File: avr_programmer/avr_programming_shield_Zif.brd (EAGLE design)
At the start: 68.6 x 53.3 mm, 16 parts

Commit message: Update after lunch session.
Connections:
- removed net N$22: ISP_85.6, U$2.3
- net N$18: now also ISP_85.6
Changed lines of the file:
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@@
 <wire x1="38.0873" y1="14.0843" x2="33.02" y2="13.9954" width="0" layer="19" extent="1-1"/>
 <wire x1="43.18" y1="13.9954" x2="38.0873" y2="14.0843" width="0" layer="19" extent="1-1"/>
+<wire x1="48.26" y1="13.97" x2="43.18" y2="13.9954" width="0" layer="19" extent="1-1"/>
+<wire x1="55.7276" y1="6.7818" x2="48.26" y2="13.97" width="0" layer="19" extent="1-1"/>
+<wire x1="62.23" y1="6.7818" x2="55.7276" y2="6.7818" width="0" layer="19" extent="1-1"/>
 <wire x1="43.561" y1="2.54" x2="43.18" y2="13.9954" width="0" layer="19" extent="1-1"/>
 <wire x1="41.021" y1="2.54" x2="43.561" y2="2.54" width="0" layer="19" extent="1-1"/>
-<wire x1="55.7276" y1="6.7818" x2="43.561" y2="2.54" width="0" layer="19" extent="1-1"/>
-<wire x1="62.23" y1="6.7818" x2="55.7276" y2="6.7818" width="0" layer="19" extent="1-1"/>
-<wire x1="48.26" y1="13.97" x2="33.02" y2="13.9954" width="0" layer="19" extent="1-1"/>
 </signal>
 <signal name="RESET">
@@
 <contactref element="ISP_84" pad="5"/>
 <contactref element="U$2" pad="4"/>
-<wire x1="34.29" y1="35.56" x2="52.07" y2="21.59" width="0" layer="19" extent="1-1"/>
+<contactref element="ISP_85" pad="6"/>
+<wire x1="45.72" y1="21.59" x2="52.07" y2="21.59" width="0" layer="19" extent="1-1"/>
+<wire x1="34.29" y1="35.56" x2="45.72" y2="21.59" width="0" layer="19" extent="1-1"/>
 </signal>
 <signal name="N$19">
@@
 <wire x1="29.21" y1="43.18" x2="43.18" y2="24.13" width="0" layer="19" extent="1-1"/>
 </signal>
-<signal name="N$22">
-<contactref element="ISP_85" pad="6"/>
-<contactref element="U$2" pad="3"/>
-<wire x1="31.75" y1="35.56" x2="45.72" y2="21.59" width="0" layer="19" extent="1-1"/>
-</signal>
 <signal name="N$14">

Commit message: Added reset cap and resonator, fixed ISP_84 MISO line.
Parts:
- added 16MHZ: RESONATORPTH, SparkFun:RESONATOR-PTH
- added C1: 10uF, SparkFun:CPOL-RADIAL-10UF-25V
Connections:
- new net N$22: 16MHZ.1, U$2.9
- new net N$25: 16MHZ.3, U$2.10
- net GND: now also 16MHZ.2
- net RESET: now also C1.2
- net VCC: now also C1.1
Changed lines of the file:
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@@
 <setting verticaltext="up"/>
 </settings>
-<grid distance="0.05" unitdist="inch" unit="inch" style="lines" multiple="1" display="yes" altdistance="0.0005" altunitdist="inch" altunit="inch"/>
+<grid distance="0.05" unitdist="inch" unit="inch" style="lines" multiple="1" display="yes" altdistance="0.005" altunitdist="inch" altunit="inch"/>
 <layers>
 <layer number="1" name="Top" color="4" fill="1" visible="yes" active="yes"/>
@@
 <element name="BNK" library="adafruit" package="LED3MM" value="" x="48.26" y="10.16" rot="R90"/>
 <element name="R4" library="adafruit" package="0204V" value="" x="49.53" y="13.97"/>
+<element name="C1" library="SparkFun" package="CPOL-RADIAL-10UF-25V" value="10uF" x="-8.89" y="3.81"/>
+<element name="16MHZ" library="SparkFun" package="RESONATOR-PTH" value="RESONATORPTH" x="-6.35" y="-3.81"/>
 </elements>
 <signals>
@@
 <contactref element="R1" pad="1"/>
 <contactref element="R4" pad="1"/>
+<contactref element="16MHZ" pad="2"/>
 <wire x1="32.9692" y1="21.8948" x2="26.797" y2="50.8" width="0" layer="19" extent="1-1"/>
 <wire x1="33.02" y1="13.9954" x2="32.9692" y2="21.8948" width="0" layer="19" extent="1-1"/>
@@
 <wire x1="43.561" y1="2.54" x2="43.18" y2="13.9954" width="0" layer="19" extent="1-1"/>
 <wire x1="41.021" y1="2.54" x2="43.561" y2="2.54" width="0" layer="19" extent="1-1"/>
+<wire x1="-6.35" y1="-3.81" x2="33.02" y2="13.9954" width="0" layer="19" extent="1-1"/>
 </signal>
 <signal name="RESET">
@@
 <contactref element="RESET" pad="3"/>
 <contactref element="U$1" pad="RESET"/>
+<contactref element="C1" pad="2"/>
 <wire x1="55.7276" y1="11.303" x2="62.23" y2="11.303" width="0" layer="19" extent="1-1"/>
-<wire x1="33.401" y1="2.54" x2="62.23" y2="11.303" width="0" layer="19" extent="1-1"/>
+<wire x1="33.401" y1="2.54" x2="55.7276" y2="11.303" width="0" layer="19" extent="1-1"/>
+<wire x1="-10.16" y1="3.81" x2="33.401" y2="2.54" width="0" layer="19" extent="1-1"/>
 </signal>
 <signal name="VIN">
@@
 <contactref element="U$1" pad="5V"/>
 <contactref element="ISP" pad="2"/>
+<contactref element="C1" pad="1"/>
 <wire x1="38.481" y1="2.54" x2="32.9692" y2="26.9748" width="0" layer="19" extent="1-1"/>
+<wire x1="-7.62" y1="3.81" x2="38.481" y2="2.54" width="0" layer="19" extent="1-1"/>
 </signal>
 <signal name="N$2">
@@
 <wire x1="63.5" y1="26.67" x2="54.61" y2="24.13" width="0" layer="19" extent="1-1"/>
 <wire x1="41.91" y1="35.56" x2="63.5" y2="26.67" width="0" layer="19" extent="1-1"/>
-</signal>
-<signal name="N$12">
-<contactref element="ISP_328" pad="6"/>
-<contactref element="U$2" pad="8"/>
-<contactref element="U$2" pad="22"/>
-<contactref element="ISP_84" pad="1"/>
-<wire x1="63.5" y1="21.59" x2="52.07" y2="26.67" width="0" layer="19" extent="1-1"/>
-<wire x1="41.91" y1="43.18" x2="63.5" y2="21.59" width="0" layer="19" extent="1-1"/>
-<wire x1="44.45" y1="35.56" x2="41.91" y2="43.18" width="0" layer="19" extent="1-1"/>
 </signal>
 <signal name="N$13">
@@
 <wire x1="33.0327" y1="8.89" x2="39.497" y2="50.8" width="0" layer="19" extent="1-1"/>
 </signal>
+<signal name="N$22">
+<contactref element="U$2" pad="9"/>
+<contactref element="16MHZ" pad="1"/>
+<wire x1="-8.89" y1="-3.81" x2="46.99" y2="35.56" width="0" layer="19" extent="1-1"/>
+</signal>
+<signal name="N$25">
+<contactref element="16MHZ" pad="3"/>
+<contactref element="U$2" pad="10"/>
+<wire x1="-3.81" y1="-3.81" x2="49.53" y2="35.56" width="0" layer="19" extent="1-1"/>
+</signal>
+<signal name="N$26">
+<contactref element="ISP_84" pad="1"/>
+<contactref element="ISP_328" pad="6"/>
+<contactref element="U$2" pad="8"/>
+<contactref element="U$2" pad="22"/>
+<wire x1="52.07" y1="26.67" x2="63.5" y2="21.59" width="0" layer="19" extent="1-1"/>
+<wire x1="44.45" y1="35.56" x2="52.07" y2="26.67" width="0" layer="19" extent="1-1"/>
+<wire x1="41.91" y1="43.18" x2="44.45" y2="35.56" width="0" layer="19" extent="1-1"/>
+</signal>
 </signals>

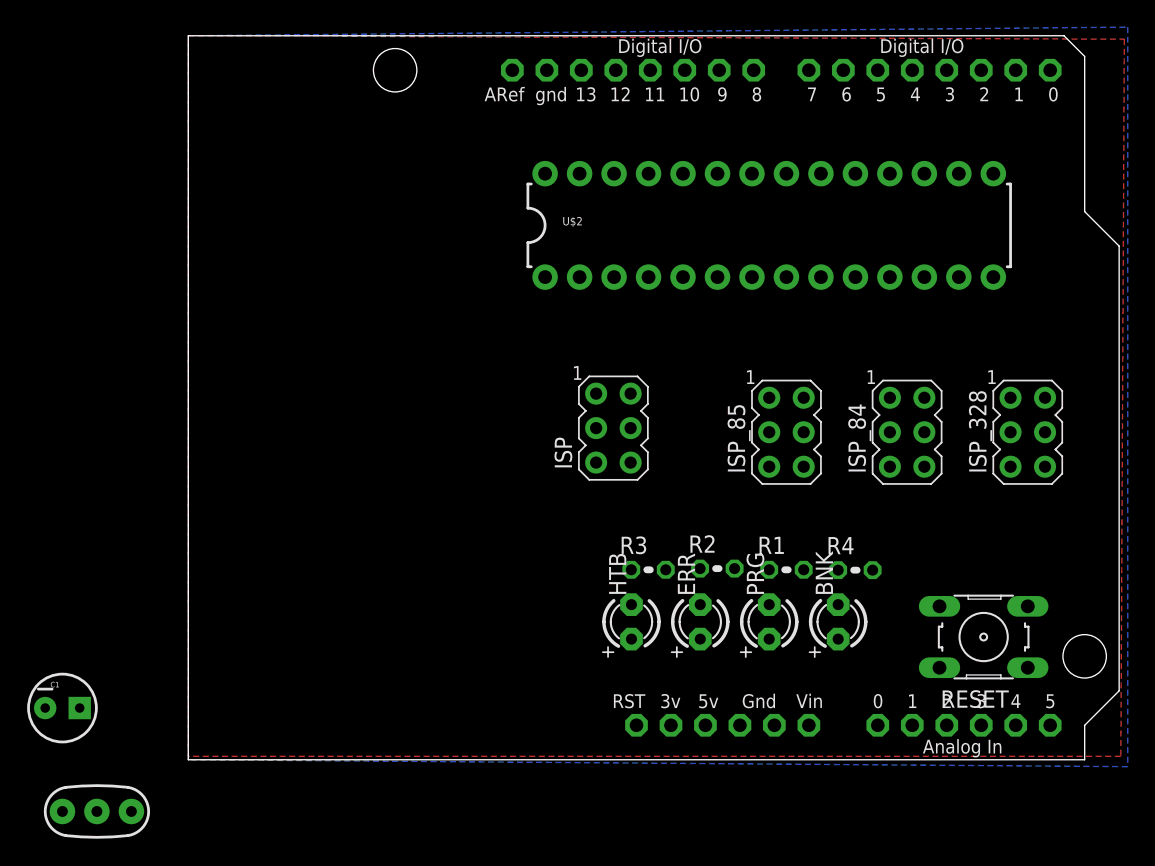
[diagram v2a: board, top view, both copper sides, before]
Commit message: Removed blink LED, added Mega jumper.
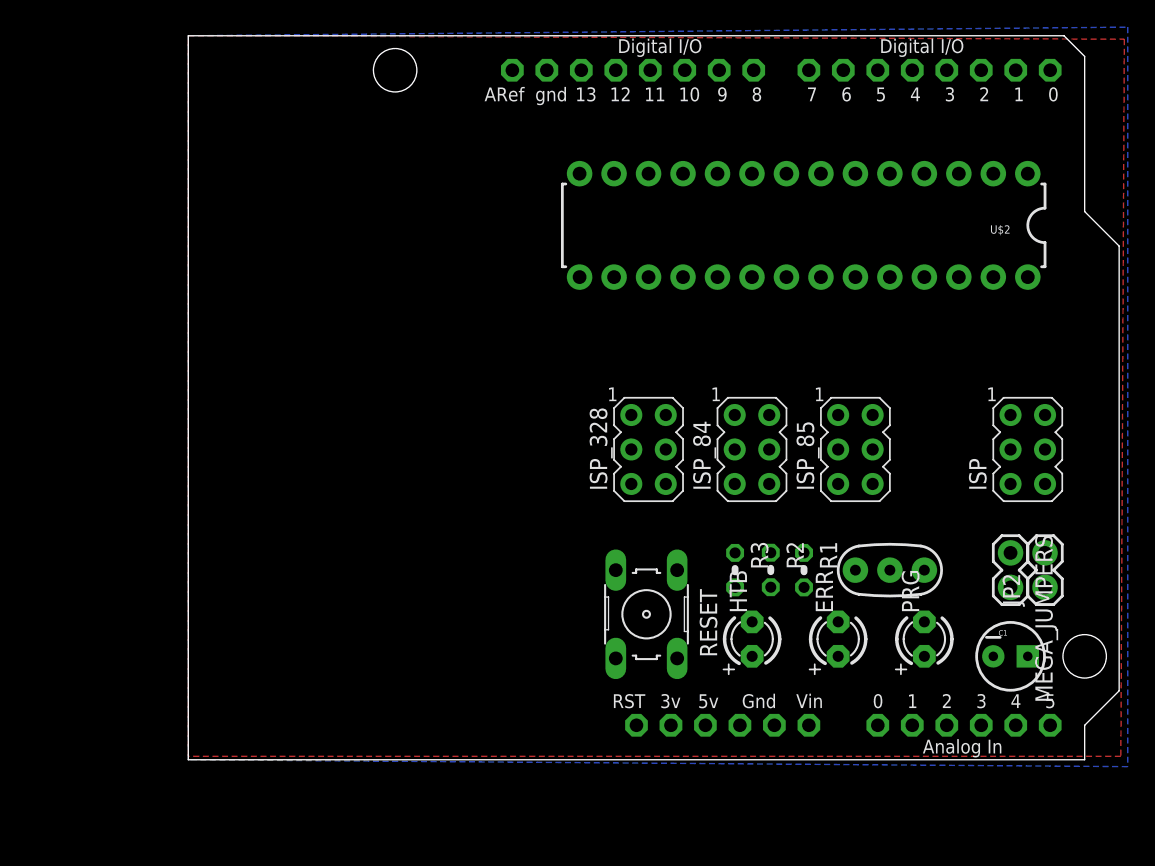
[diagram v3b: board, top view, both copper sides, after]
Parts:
- removed BNK: (no value), adafruit:LED3MM
- removed R4: (no value), adafruit:0204V
- added JP2, MEGA_JUMPERS: (no value), SparkFun:1X02
- moved C1 70.0 mm to (61.0, 7.62)
- moved 16MHZ 61.1 mm to (52.1, 14.0)
- moved ISP 30.6 mm to (62.2, 22.9)
- moved ISP_328 28.0 mm to (34.3, 22.9)
- moved RESET 24.9 mm to (34.1, 10.7), turned to 270 degrees
- moved E$1 20.7 mm to (79.5, 27.1)
- moved ISP_84 11.5 mm to (41.9, 22.9)
- moved PRG 11.5 mm to (54.6, 8.89)
- moved ERR 10.2 mm to (48.3, 8.89)
- moved HTB 8.98 mm to (41.9, 8.89)
- moved R3 6.38 mm to (40.7, 14.0), turned to 270 degrees
- moved ISP_85 5.24 mm to (49.5, 22.9)
- moved R2 3.94 mm to (43.3, 14.0), turned to 270 degrees
- moved U$2 2.54 mm to (45.7, 39.4), turned to 180 degrees
- moved R1 1.30 mm to (45.7, 14.0), turned to 270 degrees
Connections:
- removed net D3: BNK.A, U$2.2, U$2.24, U$2.5
- removed net N$14: BNK.K, R4.2
- removed net N$23: PRG.A, U$1.D7
- new net COMMON_D3: PRG.A, U$1.D7, U$2.2, U$2.24, U$2.5
- net GND: no longer R4.1
- net N$2: now also MEGA_JUMPERS.2
- net N$3: now also MEGA_JUMPERS.1
- net N$5: now also JP2.1
- net N$6: now also JP2.2

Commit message: Tweaked component layout.
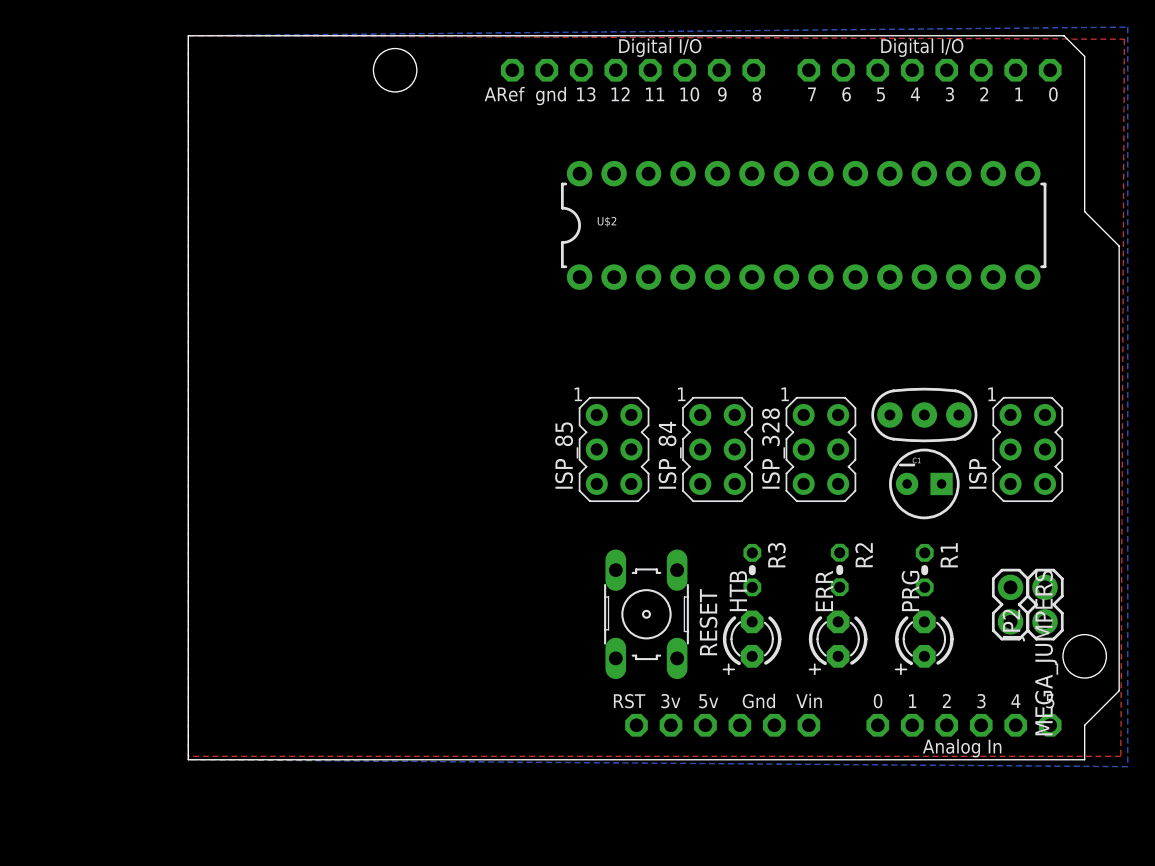
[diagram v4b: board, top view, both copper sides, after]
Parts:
- moved ISP_85 17.8 mm to (31.8, 22.9)
- moved C1 14.2 mm to (54.6, 20.3)
- moved ISP_328 12.7 mm to (47.0, 22.9)
- moved 16MHZ 11.7 mm to (54.6, 25.4)
- moved R1 8.89 mm to (54.6, 14.0)
- moved R2 5.08 mm to (48.4, 14.0)
- moved MEGA_JUMPERS 2.54 mm to (61.0, 12.7)
- moved ISP_84 2.54 mm to (39.4, 22.9)
- moved JP2 2.54 mm to (63.5, 10.2)
- moved R3 1.27 mm to (41.9, 14.0)
- turned U$2 to 0 degrees
